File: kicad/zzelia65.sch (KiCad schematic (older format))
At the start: 137 parts

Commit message: promicro & reset btn
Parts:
- added SW_Reset1: SW_Push, Button_Switch_THT:SW_PUSH_6mm, symbol Switch:SW_Push
- renumbered D_LetA1 to D_A1
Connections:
- net Col_0: now also ProMicro1.20 (F4)
- net Col_1: now also ProMicro1.19 (F5)
- net Col_2: now also ProMicro1.18 (F6)
- net Col_3: now also ProMicro1.17 (F7)
- net Col_4: now also ProMicro1.16 (B1)
- net Col_5: now also ProMicro1.15 (B3)
- net Col_6: now also ProMicro1.14 (B2)
- net Row_0: now also ProMicro1.1 (TX)
- net Row_1: now also ProMicro1.2 (RX)
- net Row_2: now also ProMicro1.5 (SDA)
- net Row_3: now also ProMicro1.6 (SCL)
- net Row_4: now also ProMicro1.7 (D4)
- net Row_5: now also ProMicro1.8 (C6)
- net Row_6: now also ProMicro1.9 (D7)
- net Row_7: now also ProMicro1.10 (E6)
- net Row_8: now also ProMicro1.11 (B4)
- net Row_9: now also ProMicro1.12 (B5)
- net RESET: now reaches ProMicro1.22 (RST)
- net RESET: now also SW_Reset1.2
- net GND: now reaches ProMicro1.23 (GND)
- net GND: now also ProMicro1.3 (GND), ProMicro1.4 (GND), SW_Reset1.1
- no-connect marks 0 -> 2
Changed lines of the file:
@@
 	1100 3250 1100 3300
 $Comp
-L Device:D_Small D_LetA1
+L Device:D_Small D_A1
 U 1 1 61B1D536
 P 1750 3400
-F 0 "D_LetA1" V 1796 3330 50  0000 R CNN
+F 0 "D_A1" V 1796 3330 50  0000 R CNN
 F 1 "D_Small" V 1705 3330 50  0000 R CNN
 F 2 "Diode_THT:D_DO-35_SOD27_P7.62mm_Horizontal" V 1750 3400 50  0001 C CNN
@@
 	1    0    0    -1
 $EndComp
+Text GLabel 1100 6450 0    50   Input ~ 0
+Row_0
+Text GLabel 1100 6550 0    50   Input ~ 0
+Row_1
+$Comp
+L power:GND #PWR0101
+U 1 1 61A97F6B
+P 600 6750
+F 0 "#PWR0101" H 600 6500 50  0001 C CNN
+F 1 "GND" H 605 6577 50  0000 C CNN
+F 2 "" H 600 6750 50  0001 C CNN
+F 3 "" H 600 6750 50  0001 C CNN
+	1    600  6750
+	1    0    0    -1
+$EndComp
+$Comp
+L power:GND #PWR0102
+U 1 1 61A997C2
+P 2950 6650
+F 0 "#PWR0102" H 2950 6400 50  0001 C CNN
+F 1 "GND" H 2955 6477 50  0000 C CNN
+F 2 "" H 2950 6650 50  0001 C CNN
+F 3 "" H 2950 6650 50  0001 C CNN
+	1    2950 6650
+	1    0    0    -1
+$EndComp
+NoConn ~ 2500 6450
+$Comp
+L Switch:SW_Push SW_Reset1
+U 1 1 61AC615F
+P 4500 6550
+F 0 "SW_Reset1" H 4500 6835 50  0000 C CNN
+F 1 "SW_Push" H 4500 6744 50  0000 C CNN
+F 2 "Button_Switch_THT:SW_PUSH_6mm" H 4500 6750 50  0001 C CNN
+F 3 "~" H 4500 6750 50  0001 C CNN
+	1    4500 6550
+	1    0    0    -1
+$EndComp
+$Comp
+L power:GND #PWR0103
+U 1 1 61AC7D88
+P 4100 6650
+F 0 "#PWR0103" H 4100 6400 50  0001 C CNN
+F 1 "GND" H 4105 6477 50  0000 C CNN
+F 2 "" H 4100 6650 50  0001 C CNN
+F 3 "" H 4100 6650 50  0001 C CNN
+	1    4100 6650
+	1    0    0    -1
+$EndComp
+Text GLabel 4700 6550 2    50   Input ~ 0
+RESET
+Text GLabel 1100 6850 0    50   Input ~ 0
+Row_2
+Text GLabel 1100 6950 0    50   Input ~ 0
+Row_3
+Text GLabel 1100 7050 0    50   Input ~ 0
+Row_4
+Text GLabel 1100 7150 0    50   Input ~ 0
+Row_5
+Text GLabel 1100 7250 0    50   Input ~ 0
+Row_6
+Text GLabel 1100 7350 0    50   Input ~ 0
+Row_7
+Text GLabel 1100 7450 0    50   Input ~ 0
+Row_8
+Text GLabel 1100 7550 0    50   Input ~ 0
+Row_9
+Text GLabel 2500 6650 2    50   Input ~ 0
+RESET
+NoConn ~ 2500 6750
+Text GLabel 2500 6850 2    50   Input ~ 0
+Col_0
+Text GLabel 2500 6950 2    50   Input ~ 0
+Col_1
+Text GLabel 2500 7050 2    50   Input ~ 0
+Col_2
+Text GLabel 2500 7150 2    50   Input ~ 0
+Col_3
+Text GLabel 2500 7250 2    50   Input ~ 0
+Col_4
+Text GLabel 2500 7350 2    50   Input ~ 0
+Col_5
+Text GLabel 2500 7450 2    50   Input ~ 0
+Col_6
+Wire Wire Line
+	2500 6550 2950 6550
+Wire Wire Line
+	2950 6550 2950 6650
+Wire Wire Line
+	600  6750 1100 6750
+Wire Wire Line
+	1100 6650 600  6650
+Wire Wire Line
+	600  6650 600  6750
+Connection ~ 600  6750
+Wire Wire Line
+	4300 6550 4100 6550
+Wire Wire Line
+	4100 6550 4100 6650
 $EndSCHEMATC

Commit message: 18-pin
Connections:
- net Col_0: no longer K_Back1.1 (COL), K_Backslash1.1 (COL), K_End1.1 (COL), K_Home1.1 (COL), K_Insert1.1 (COL)
- net Col_1: now also K_End1.1 (COL), K_Home1.1 (COL), K_Insert1.1 (COL), K_Right1.1 (COL); no longer K_Close1.1 (COL), K_Enter1.1 (COL), K_Plus1.1 (COL), K_Up1.1 (COL)
- net Col_2: now also K_Back1.1 (COL), K_Backslash1.1 (COL), K_Down1.1 (COL), K_Enter1.1 (COL), K_Up1.1 (COL); no longer K_Minus1.1 (COL), K_Open1.1 (COL), K_Quote1.1 (COL), K_RShift1.1 (COL), K_Right1.1 (COL)
- net Col_3: now also K_Close1.1 (COL), K_Left1.1 (COL), K_Plus1.1 (COL), K_Quote1.1 (COL), K_RShift1.1 (COL); no longer K_0.1 (COL), K_Down1.1 (COL), K_P1.1 (COL), K_Semi1.1 (COL), K_Slash1.1 (COL)
- net Col_4: now also K_Minus1.1 (COL), K_Open1.1 (COL), K_RCtrl1.1 (COL), K_Semi1.1 (COL), K_Slash1.1 (COL); no longer K_9.1 (COL), K_Dot1.1 (COL), K_L1.1 (COL), K_Left1.1 (COL), K_O1.1 (COL)
- net Col_5: now also K_0.1 (COL), K_Dot1.1 (COL), K_L1.1 (COL), K_P1.1 (COL); no longer K_8.1 (COL), K_Comma1.1 (COL), K_I1.1 (COL), K_K1.1 (COL), K_RCtrl1.1 (COL)
- net Col_6: now also K_9.1 (COL), K_Comma1.1 (COL), K_K1.1 (COL), K_O1.1 (COL); no longer K_7.1 (COL), K_J1.1 (COL), K_M1.1 (COL), K_U1.1 (COL)
- net Row_0: now also D_7.1 (K)
- net Row_1: now also D_U1.1 (K)
- net Row_2: now also D_J1.1 (K)
- net Row_3: now also D_M1.1 (K)
- net Row_5: no longer D_Del1.1 (K), D_End1.1 (K)
- net Row_6: now also D_Del1.1 (K); no longer D_Home1.1 (K), D_M1.1 (K)
- net Row_7: now also D_End1.1 (K); no longer D_Insert1.1 (K), D_J1.1 (K)
- net Row_8: now also D_Home1.1 (K); no longer D_U1.1 (K)
- net Row_9: now also D_Insert1.1 (K); no longer D_7.1 (K)
- net Col_7: now reaches ProMicro1.13 (B6)
- net Col_7: now also K_7.1 (COL), K_8.1 (COL), K_I1.1 (COL), K_J1.1 (COL), K_M1.1 (COL), K_U1.1 (COL)
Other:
- moved on the sheet: D_0, D_1, D_2, D_3, D_4, D_5, D_6, D_7, D_8, D_9, D_A1, D_B1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

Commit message: routing
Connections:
- net Col_1: now also ProMicro1.13 (B6); no longer ProMicro1.19 (F5)
- net Col_2: now also ProMicro1.14 (B2); no longer ProMicro1.18 (F6)
- net Col_3: now also ProMicro1.15 (B3); no longer ProMicro1.17 (F7)
- net Col_5: now also ProMicro1.17 (F7); no longer ProMicro1.15 (B3)
- net Col_6: now also ProMicro1.18 (F6); no longer ProMicro1.14 (B2)
- net Col_7: now also ProMicro1.19 (F5); no longer ProMicro1.13 (B6)
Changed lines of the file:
@@
 Text GLabel 2500 6850 2    50   Input ~ 0
 Col_0
-Text GLabel 2500 6950 2    50   Input ~ 0
+Text GLabel 2500 7550 2    50   Input ~ 0
 Col_1
-Text GLabel 2500 7050 2    50   Input ~ 0
+Text GLabel 2500 7450 2    50   Input ~ 0
 Col_2
-Text GLabel 2500 7150 2    50   Input ~ 0
+Text GLabel 2500 7350 2    50   Input ~ 0
 Col_3
 Text GLabel 2500 7250 2    50   Input ~ 0
 Col_4
-Text GLabel 2500 7350 2    50   Input ~ 0
+Text GLabel 2500 7150 2    50   Input ~ 0
 Col_5
-Text GLabel 2500 7450 2    50   Input ~ 0
+Text GLabel 2500 7050 2    50   Input ~ 0
 Col_6
 Wire Wire Line
@@
 	10700 5050 10700 5800
 Connection ~ 1900 5050
-Text GLabel 2500 7550 2    50   Input ~ 0
+Text GLabel 2500 6950 2    50   Input ~ 0
 Col_7
 $EndSCHEMATC

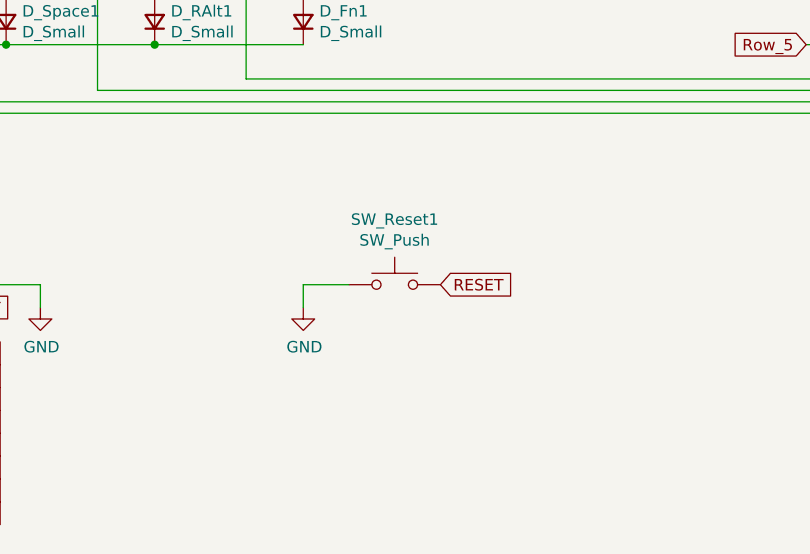
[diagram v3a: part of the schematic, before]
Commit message: remove reset button
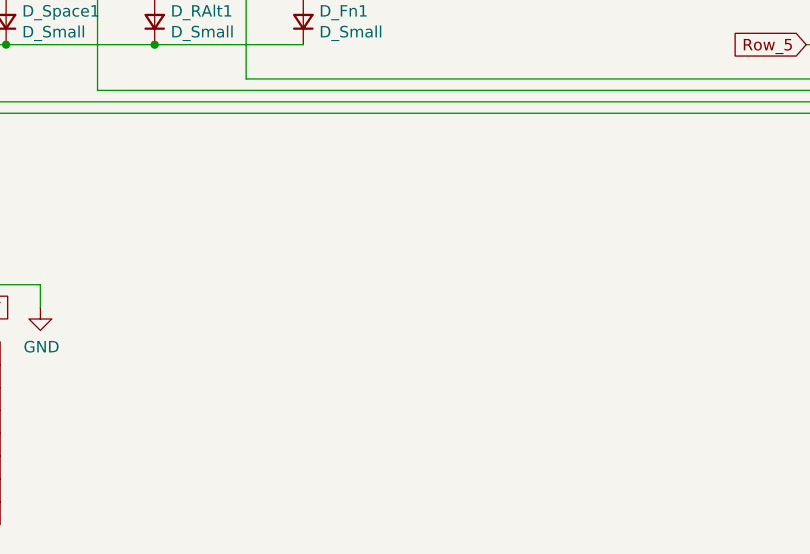
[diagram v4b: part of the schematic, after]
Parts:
- removed SW_Reset1: SW_Push, Button_Switch_THT:SW_PUSH_6mm, symbol Switch:SW_Push
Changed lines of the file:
@@
 $EndComp
 NoConn ~ 2500 6450
-$Comp
-L Switch:SW_Push SW_Reset1
-U 1 1 61AC615F
-P 4500 6550
-F 0 "SW_Reset1" H 4500 6835 50  0000 C CNN
-F 1 "SW_Push" H 4500 6744 50  0000 C CNN
-F 2 "Button_Switch_THT:SW_PUSH_6mm" H 4500 6750 50  0001 C CNN
-F 3 "~" H 4500 6750 50  0001 C CNN
-	1    4500 6550
-	1    0    0    -1
-$EndComp
-$Comp
-L power:GND #PWR0103
-U 1 1 61AC7D88
-P 4100 6650
-F 0 "#PWR0103" H 4100 6400 50  0001 C CNN
-F 1 "GND" H 4105 6477 50  0000 C CNN
-F 2 "" H 4100 6650 50  0001 C CNN
-F 3 "" H 4100 6650 50  0001 C CNN
-	1    4100 6650
-	1    0    0    -1
-$EndComp
-Text GLabel 4700 6550 2    50   Input ~ 0
-RESET
 Text GLabel 1100 6850 0    50   Input ~ 0
 Row_2
@@
 Connection ~ 600  6750
 Wire Wire Line
-	4300 6550 4100 6550
-Wire Wire Line
-	4100 6550 4100 6650
-Wire Wire Line
 	750  1500 850  1500

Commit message: reset button
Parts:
- added Reset1: RESET, Button_Switch_THT:SW_PUSH_6mm, symbol Switch:SW_Push
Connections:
- net GND: now also Reset1.1
- net RESET: now also Reset1.2
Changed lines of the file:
@@
 Text GLabel 2500 6950 2    50   Input ~ 0
 Col_7
+$Comp
+L Switch:SW_Push Reset1
+U 1 1 61B0A3A6
+P 4000 6300
+F 0 "Reset1" H 4000 6585 50  0000 C CNN
+F 1 "RESET" H 4000 6494 50  0000 C CNN
+F 2 "Button_Switch_THT:SW_PUSH_6mm" H 4000 6500 50  0001 C CNN
+F 3 "~" H 4000 6500 50  0001 C CNN
+	1    4000 6300
+	1    0    0    -1
+$EndComp
+Text GLabel 4200 6300 2    50   Input ~ 0
+RESET
+$Comp
+L power:GND #PWR0103
+U 1 1 61B0DF5D
+P 3800 6400
+F 0 "#PWR0103" H 3800 6150 50  0001 C CNN
+F 1 "GND" H 3805 6227 50  0000 C CNN
+F 2 "" H 3800 6400 50  0001 C CNN
+F 3 "" H 3800 6400 50  0001 C CNN
+	1    3800 6400
+	1    0    0    -1
+$EndComp
+Wire Wire Line
+	3800 6300 3800 6400
 $EndSCHEMATC
